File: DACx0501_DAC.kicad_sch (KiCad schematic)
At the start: 7 parts, among them U3 DACx0501

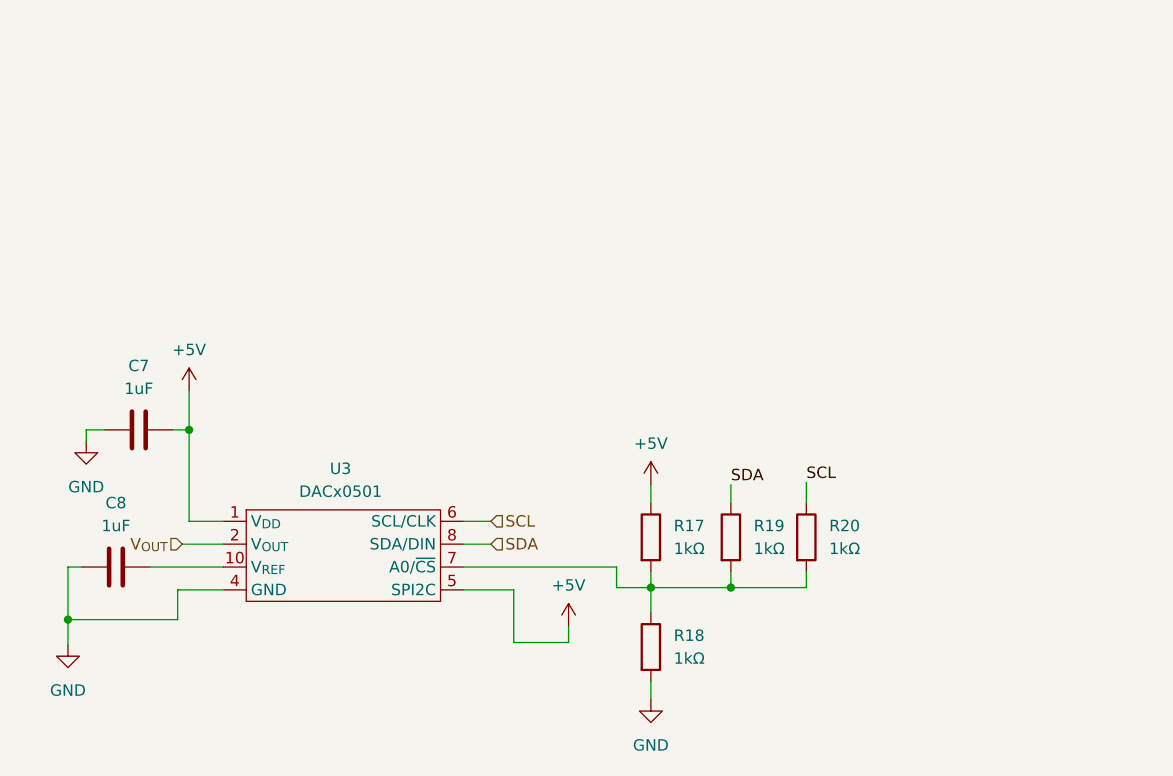
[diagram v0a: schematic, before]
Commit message: Added extra capacitor and reroute the power to better optimize the board.
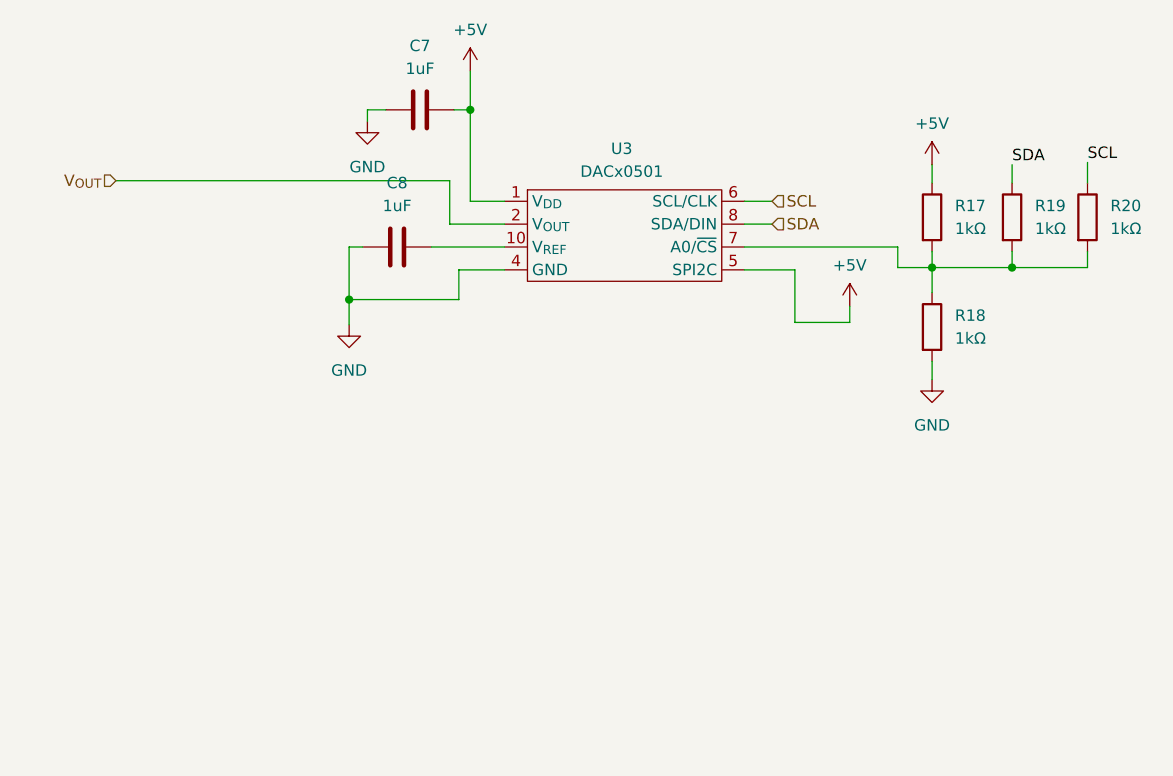
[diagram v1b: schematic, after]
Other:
- moved on the sheet: C7, C8, R17, R18, R19, R20, U3
